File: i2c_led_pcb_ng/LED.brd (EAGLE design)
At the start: 53.6 x 27.5 mm, 47 parts

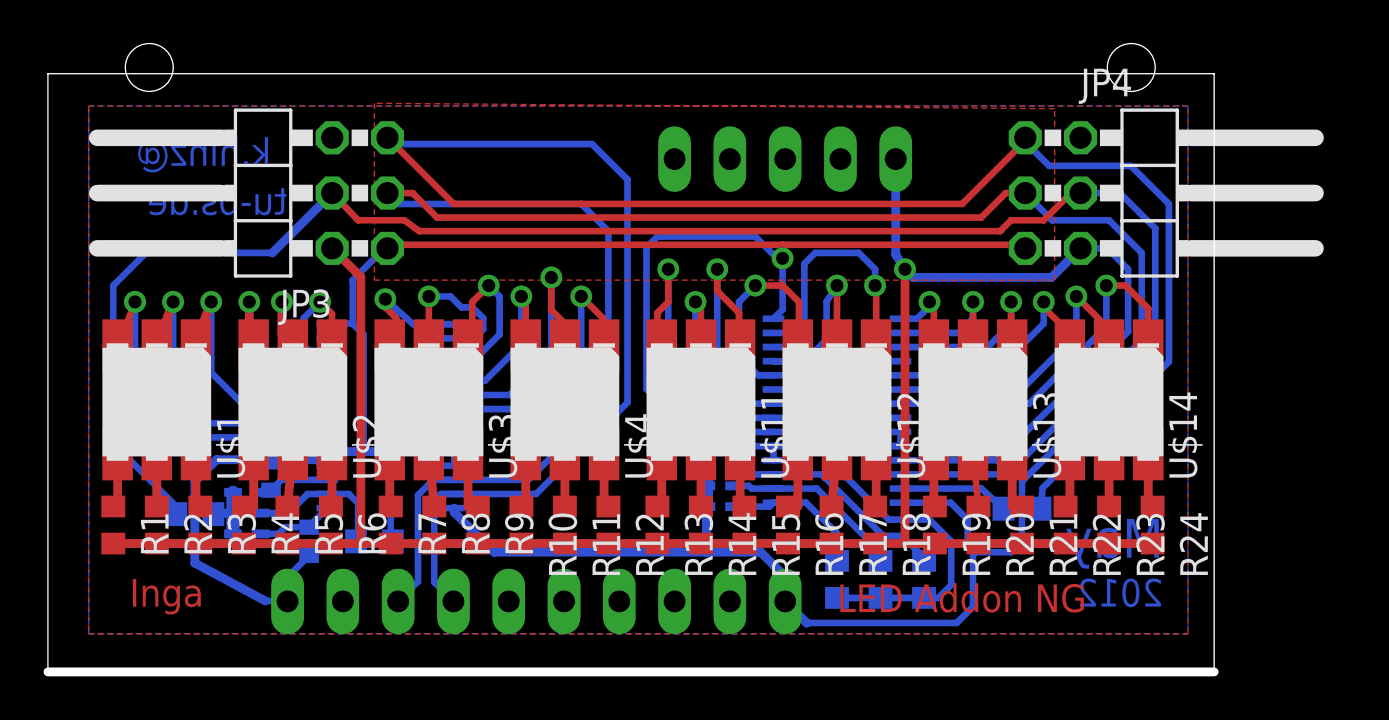
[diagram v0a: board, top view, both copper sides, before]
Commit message: moved connector; bigger LED-pads for cooling; smaller address selector
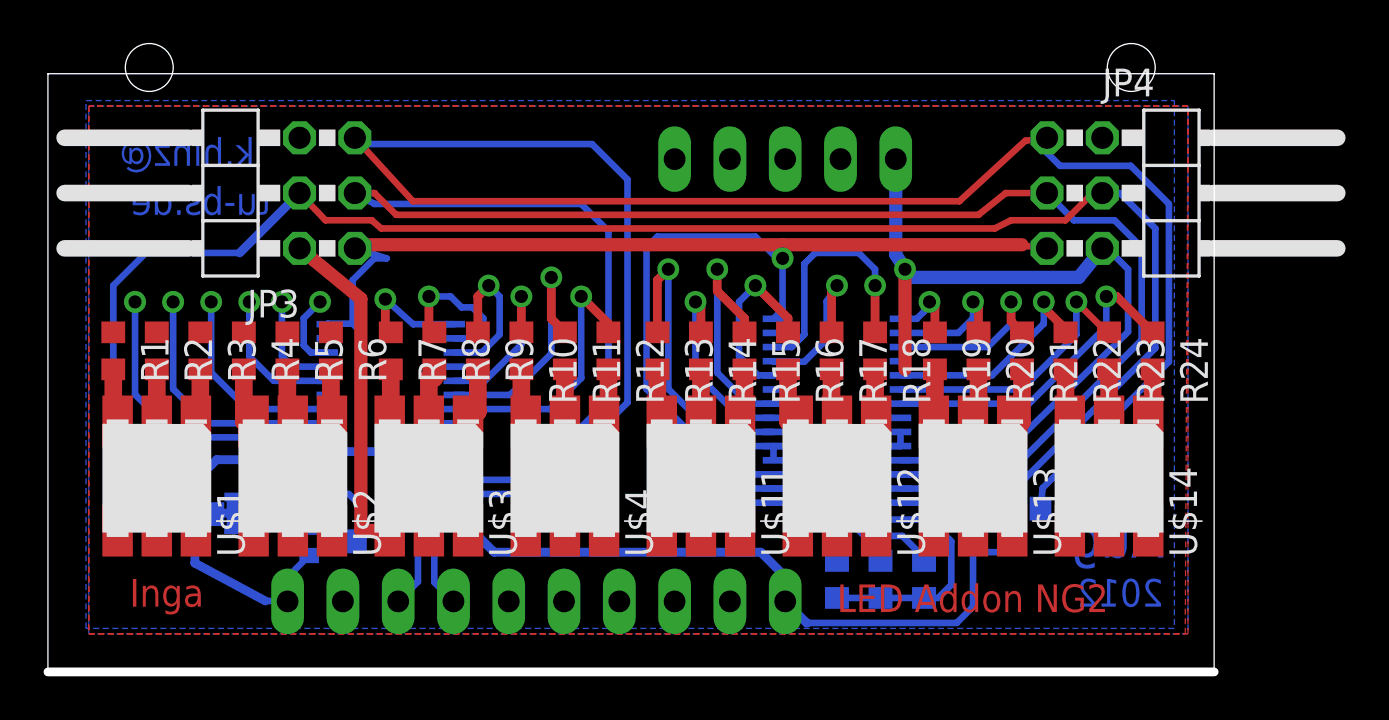
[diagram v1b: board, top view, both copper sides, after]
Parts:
- moved R1 8.00 mm to (2.25, 14.2)
- moved R10 8.00 mm to (21.0, 14.2)
- moved R11 8.00 mm to (23.0, 14.2)
- moved R12 8.00 mm to (25.0, 14.2)
- moved R13 8.00 mm to (27.2, 14.2)
- moved R14 8.00 mm to (29.2, 14.2)
- moved R15 8.00 mm to (31.2, 14.2)
- moved R16 8.00 mm to (33.2, 14.2)
- moved R17 8.00 mm to (35.2, 14.2)
- moved R18 8.00 mm to (37.2, 14.2)
- moved R19 8.00 mm to (40.0, 14.2)
- moved R2 8.00 mm to (4.25, 14.2)
- moved R20 8.00 mm to (42.0, 14.2)
- moved R21 8.00 mm to (44.0, 14.2)
- moved R22 8.00 mm to (46.0, 14.2)
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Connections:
- net +3V3: no longer ADDR_SEL1.VCC, ADDR_SEL1.VCC@1, ADDR_SEL1.VCC@2
- net N$1: now also R1.1; no longer U$1.P3
- net N$10: now also R10.1; no longer U$4.P3
- net N$11: now also R11.1; no longer U$4.P2
- net N$12: now also R12.1; no longer U$4.P1
- net N$13: now also R12.2, U$4.P1; no longer R3.1, U$1.P6
- net N$14: now also R11.2, U$4.P2; no longer R2.1, U$1.P5
- net N$15: now also R10.2, U$4.P3; no longer R1.1, U$1.P4
- net N$17: now also R7.2, U$3.P3; no longer R6.1, U$2.P6
- net N$18: now also R8.2, U$3.P2; no longer R5.1, U$2.P5
- net N$19: now also R2.2, U$1.P2; no longer R4.1, U$2.P4
- net N$2: now also R2.1; no longer U$1.P2
- net N$20: now also R1.2, U$1.P3; no longer R9.1, U$3.P6
- net N$21: now also R3.2, U$1.P1; no longer R8.1, U$3.P5
- net N$22: now also R4.2, U$2.P3; no longer R7.1, U$3.P4
- net N$23: now also R5.2, U$2.P2; no longer R12.1, U$4.P6
- net N$24: now also R6.2, U$2.P1; no longer R11.1, U$4.P5
- net N$25: now also R13.2, U$11.P3; no longer R10.1, U$4.P4
- net N$26: now also R13.1; no longer U$11.P3
- net N$27: now also R14.1; no longer U$11.P2
- net N$28: now also R15.1; no longer U$11.P1
- net N$29: now also R16.1; no longer U$12.P3
- net N$3: now also R3.1; no longer U$1.P1
- net N$30: now also R17.1; no longer U$12.P2
- net N$31: now also R18.1; no longer U$12.P1
- net N$32: now also R19.1; no longer U$13.P3
- net N$33: now also R20.1; no longer U$13.P2
- net N$34: now also R21.1; no longer U$13.P1
- net N$35: now also R22.1; no longer U$14.P3
- net N$36: now also R23.1; no longer U$14.P2
- net N$37: now also R24.1; no longer U$14.P1
- net N$38: now also R14.2, U$11.P2; no longer R15.1, U$11.P6
- net N$39: now also R15.2, U$11.P1; no longer R14.1, U$11.P5
- net N$4: now also R4.1; no longer U$2.P3
- net N$40: now also R16.2, U$12.P3; no longer R13.1, U$11.P4
- net N$41: now also R17.2, U$12.P2; no longer R18.1, U$12.P6
- net N$42: now also R18.2, U$12.P1; no longer R17.1, U$12.P5
- net N$43: now also R24.2, U$14.P1; no longer R16.1, U$12.P4
- net N$44: now also R23.2, U$14.P2; no longer R21.1, U$13.P6
- net N$45: now also R22.2, U$14.P3; no longer R20.1, U$13.P5
- net N$46: now also R21.2, U$13.P1; no longer R19.1, U$13.P4
- net N$47: now also R20.2, U$13.P2; no longer R24.1, U$14.P6
- net N$48: now also R19.2, U$13.P3; no longer R23.1, U$14.P5
- net N$49: now also R9.2, U$3.P1; no longer R22.1, U$14.P4
- net N$5: now also R5.1; no longer U$2.P2
- net N$6: now also R6.1; no longer U$2.P1
- net N$7: now also R7.1; no longer U$3.P3
- net N$8: now also R8.1; no longer U$3.P2
- net N$9: now also R9.1; no longer U$3.P1
- net VCC: now also ADDR_SEL1.VCC, ADDR_SEL1.VCC@1, ADDR_SEL1.VCC@2, U$1.P4, U$1.P5, U$1.P6, U$11.P4, U$11.P5, U$11.P6, U$12.P4, U$12.P5, U$12.P6, U$13.P4, U$13.P5, U$13.P6, U$14.P4, U$14.P5, U$14.P6, U$2.P4, U$2.P5, U$2.P6, U$3.P4, U$3.P5, U$3.P6, U$4.P4, U$4.P5, U$4.P6; no longer R1.2, R10.2, R11.2, R12.2, R13.2, R14.2, R15.2, R16.2, R17.2, R18.2, R19.2, R2.2, R20.2, R21.2, R22.2, R23.2, R24.2, R3.2, R4.2, R5.2, R6.2, R7.2, R8.2, R9.2
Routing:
- net VCC: track 106.7 -> 54.1 mm
- net GND: track 117.7 -> 121.2 mm
- net +3V3: track 120.5 -> 117.3 mm
- net SDA: track 94.0 -> 97.1 mm
- net SCL: track 88.8 -> 91.7 mm
- net N$6: track 5.76 -> 3.53 mm
- net N$5: track 6.99 -> 4.78 mm
- net N$1: track 16.1 -> 13.9 mm
- net N$3: track 11.4 -> 9.28 mm
- net N$2: track 13.9 -> 11.7 mm
- net N$4: track 8.63 -> 6.55 mm
- net N$37: track 16.9 -> 15.1 mm
- net N$29: track 9.84 -> 8.28 mm
- net N$36: track 13.7 -> 12.7 mm
- net BLA: track 1.87 -> 0.83 mm
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- added copper zone on layer 16, net N$50
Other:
- board text added: "Aug"
- board text added: "LED Addon NG2"
- board text removed: "LED Addon NG"
- board text removed: "May"
